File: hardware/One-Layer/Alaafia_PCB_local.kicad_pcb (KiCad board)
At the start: 2 copper layers, 70.9 x 51.5 mm, 6 parts, among them J1 BATTERY, U1 ESP32-C3_SUPERMINI, U2 BMI160, U3 MT3608

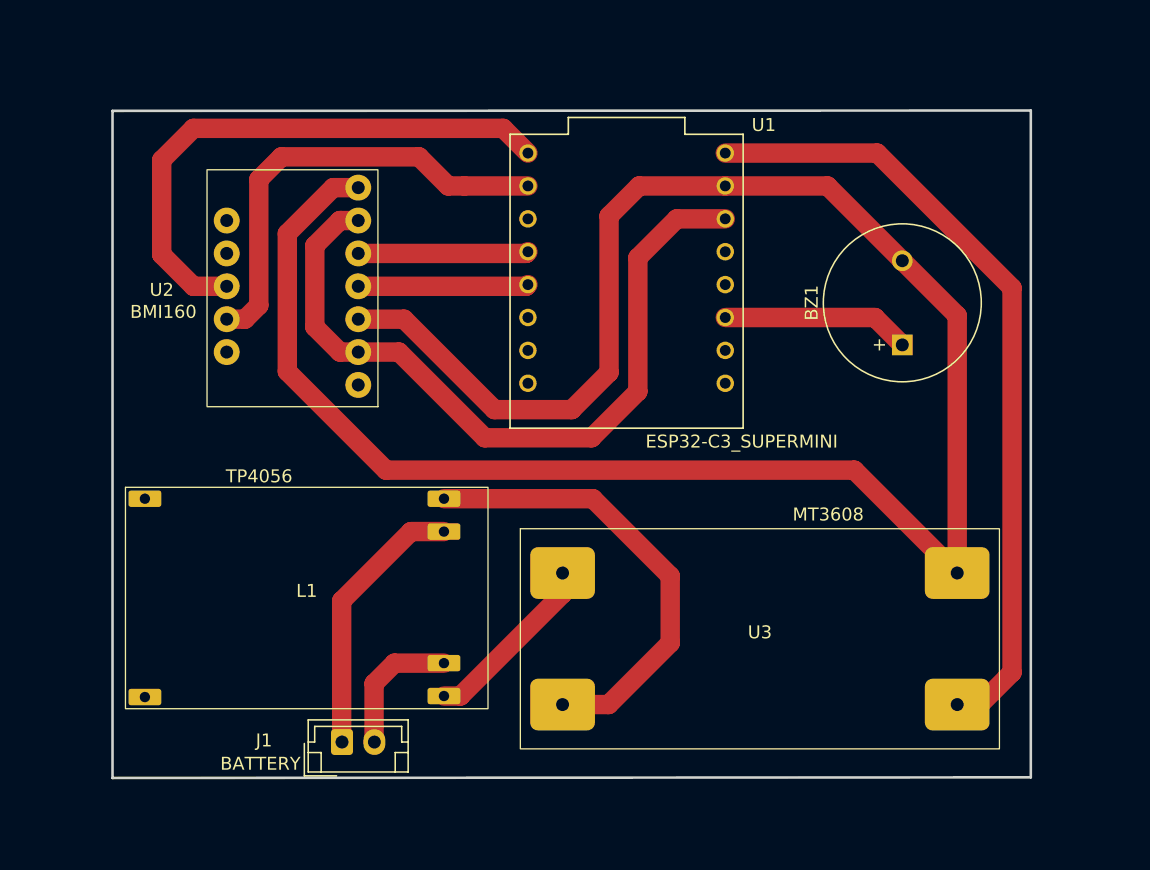
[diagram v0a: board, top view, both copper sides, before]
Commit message: Local PCB with button and SIM JST
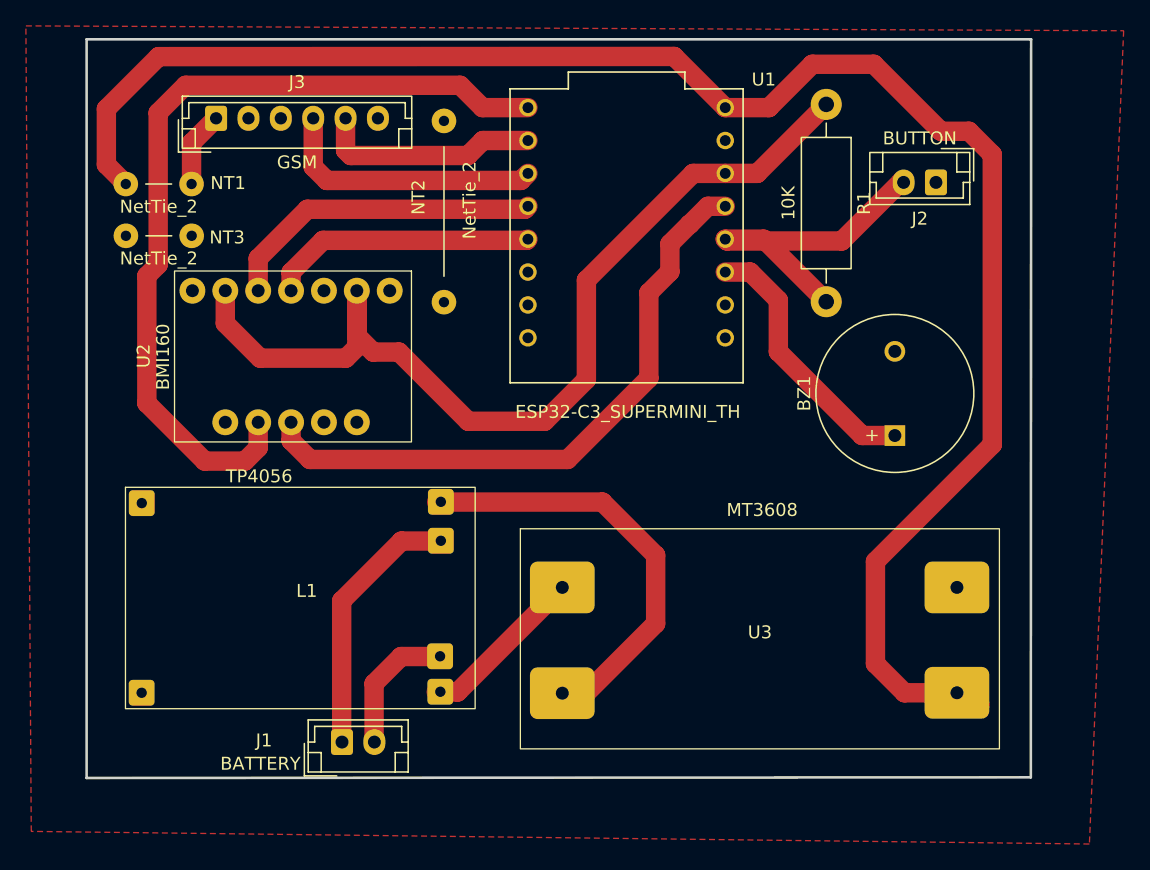
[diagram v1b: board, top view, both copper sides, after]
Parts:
- added J2: BUTTON, Connector_JST:JST_EH_B2B-EH-A_1x02_P2.50mm_Vertical, F.Cu at (177.1, 60.2)
- added J3: GSM, Connector_JST:JST_EH_B6B-EH-A_1x06_P2.50mm_Vertical, F.Cu at (121.5, 55.3)
- added NT1: NetTie_2, PCM_SL_Jumpers:JUP_P5.08mm, F.Cu at (117.1, 60.4)
- added NT2: NetTie_2, PCM_SL_Jumpers:JUP_P14mm, F.Cu at (139.1, 62.5)
- added NT3: NetTie_2, PCM_SL_Jumpers:JUP_P5.08mm, F.Cu at (117.1, 64.4)
- added R1: 10K, Resistor_THT:R_Axial_DIN0411_L9.9mm_D3.6mm_P15.24mm_Horizontal, F.Cu at (168.6, 54.2)
- U1: value ESP32-C3_SUPERMINI -> ESP32-C3_SUPERMINI_TH
- moved BZ1 7.02 mm to (173.9, 79.8)
- moved U2 5.42 mm to (127.3, 73.7), turned to -90 degrees
- moved U1 3.51 mm to (153.2, 64.4)
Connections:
- BZ1 pad 2: /GND -> GND
- J1 pad 1: Net-(L1-B+) -> Net-(L1-B-)
- J1 pad 2: Net-(L1-B-) -> Net-(L1-B-)_1
- L1 pad 1: Net-(L1-OUT+) -> unconnected-(L1-IN+-Pad1)
- L1 pad 2: Net-(L1-OUT-) -> unconnected-(L1-IN--Pad2)
- L1 pad 3: Net-(L1-B+) -> Net-(L1-OUT+)
- L1 pad 5: unconnected-(L1-IN+-Pad5) -> Net-(L1-B-)_1
- L1 pad 6: unconnected-(L1-IN--Pad6) -> Net-(L1-OUT-)
- U1 pad 3: unconnected-(U1-GPIO3-Pad3) -> /BUTTON
- U1 pad 4: unconnected-(U1-GPIO4-Pad4) -> /INT1
- U1 pad 5: /INT1 -> /INT2
- U1 pad 6: /INT2 -> /SIM_TXD
- U1 pad 7: unconnected-(U1-GPIO7-Pad7) -> /SIM_RXD
- U1 pad G: /GND -> GND
- U2 pad 11: /INT2 -> unconnected-(U2-SCX-Pad11)
- U2 pad 3: /GND -> GND
- U2 pad 7: /GND -> GND
- U2 pad 9: unconnected-(U2-SCX-Pad9) -> /INT2
- U3 pad 1: Net-(L1-OUT+) -> /5V
- U3 pad 2: Net-(L1-OUT-) -> GND
- U3 pad 3: /5V -> Net-(L1-OUT+)
- U3 pad 4: /GND -> Net-(L1-OUT-)
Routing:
- net /GND: track 163.2 -> 0.00 mm
- net /5V: track 61.4 -> 140.3 mm
- net /INT2: track 35.1 -> 65.8 mm
- net /BUTTON: track 0.00 -> 25.5 mm
- net Net-(L1-B+): track 21.0 -> 0.00 mm
- net /SIM_RXD: track 0.00 -> 21.0 mm
- net /SIM_TXD: track 0.00 -> 17.2 mm
- net /3V3: track 58.7 -> 75.6 mm
- net /SDA: track 13.2 -> 25.0 mm
- net Net-(L1-B-)_1: track 0.00 -> 10.2 mm
- net Net-(L1-B-): track 10.6 -> 20.2 mm
- net /SCL: track 13.2 -> 20.8 mm
- net Net-(U1-GPIO2): track 14.7 -> 20.7 mm
- net /INT1: track 43.4 -> 48.8 mm
- net Net-(L1-OUT-): track 14.0 -> 13.1 mm
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- added copper zone on F.Cu, net GND
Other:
- board size 70.9 x 51.5 mm -> 72.9 x 57 mm
